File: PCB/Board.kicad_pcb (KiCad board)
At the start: 2 copper layers, 80 x 40 mm, 3 parts, among them Q2 IRF9540N, U1 ESP32-C3-SuperMini

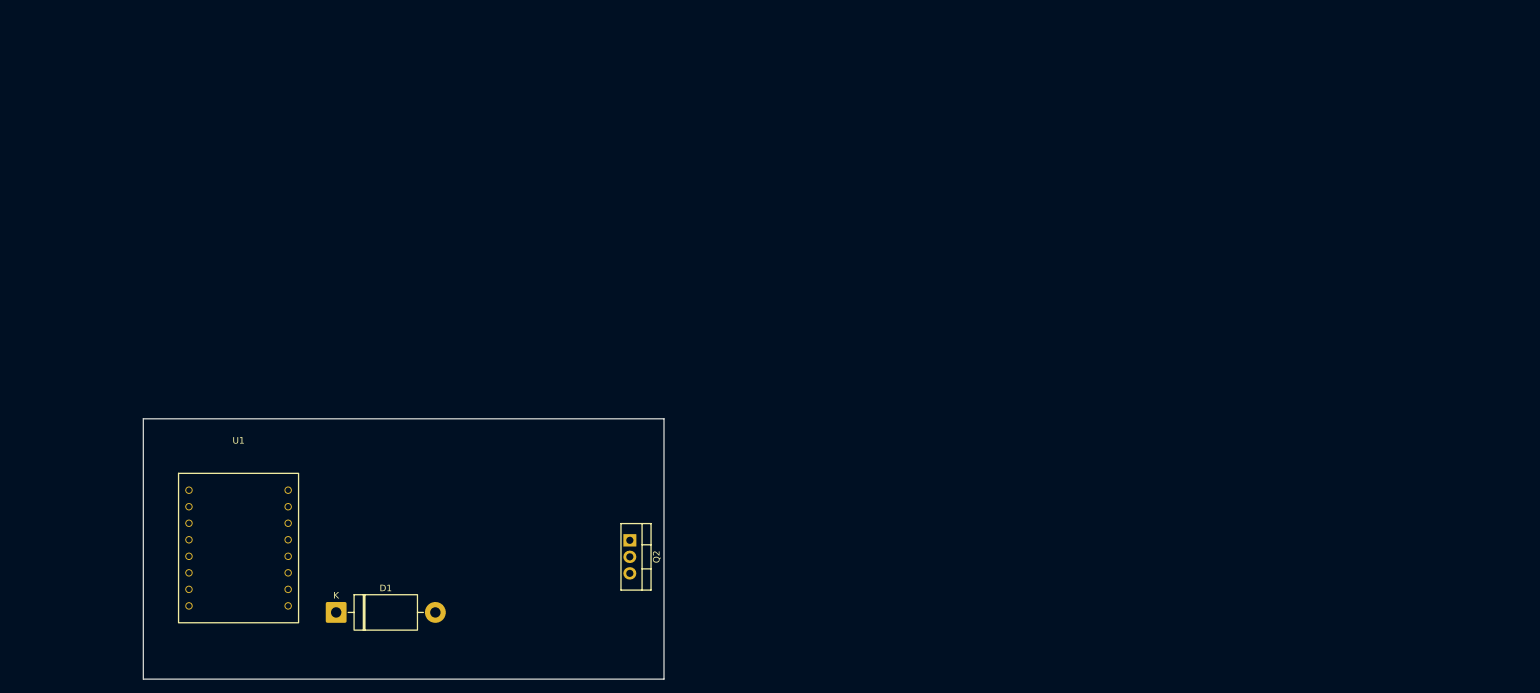
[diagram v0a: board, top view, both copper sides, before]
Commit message: PCB: fix and localize 3D models for all footprints
- Fix Q2 (SparkFun TO-220-3 footprint): model path used the
  nonexistent ${KICAD9_3RD_PARTY} env var instead of
  ${KICAD10_3RD_PARTY}, leaving it unresolved on KiCad 10.
- Fix J1 (TerminalBlock_MaiXu_MX126-5.0-02P): no 3D model exists for
  this footprint anywhere, including upstream (see kicad-packages3D
  issue #442, "Missing Terminal Blocks 3D"). Substituted the closest
  match already in KiCad's library: TerminalBlock_Phoenix
  PT-1,5-2-5.0-H (same pin count, pitch, and orientation).
- Copy every model actually used by the board (resistor, diode,
  buzzer, TO-92L, both TO-220-3 variants, IRF9Z34N, SparkFun TO-220-3,
  Phoenix terminal block, ESP32-C3-SuperMini) into PCB/3d_models/ and
  repoint all (model ...) references at ${KIPRJMOD}/3d_models/..., so
  the board no longer depends on system libraries, PCM 3rd-party
  installs, or a user's ~/Downloads folder to render correctly.
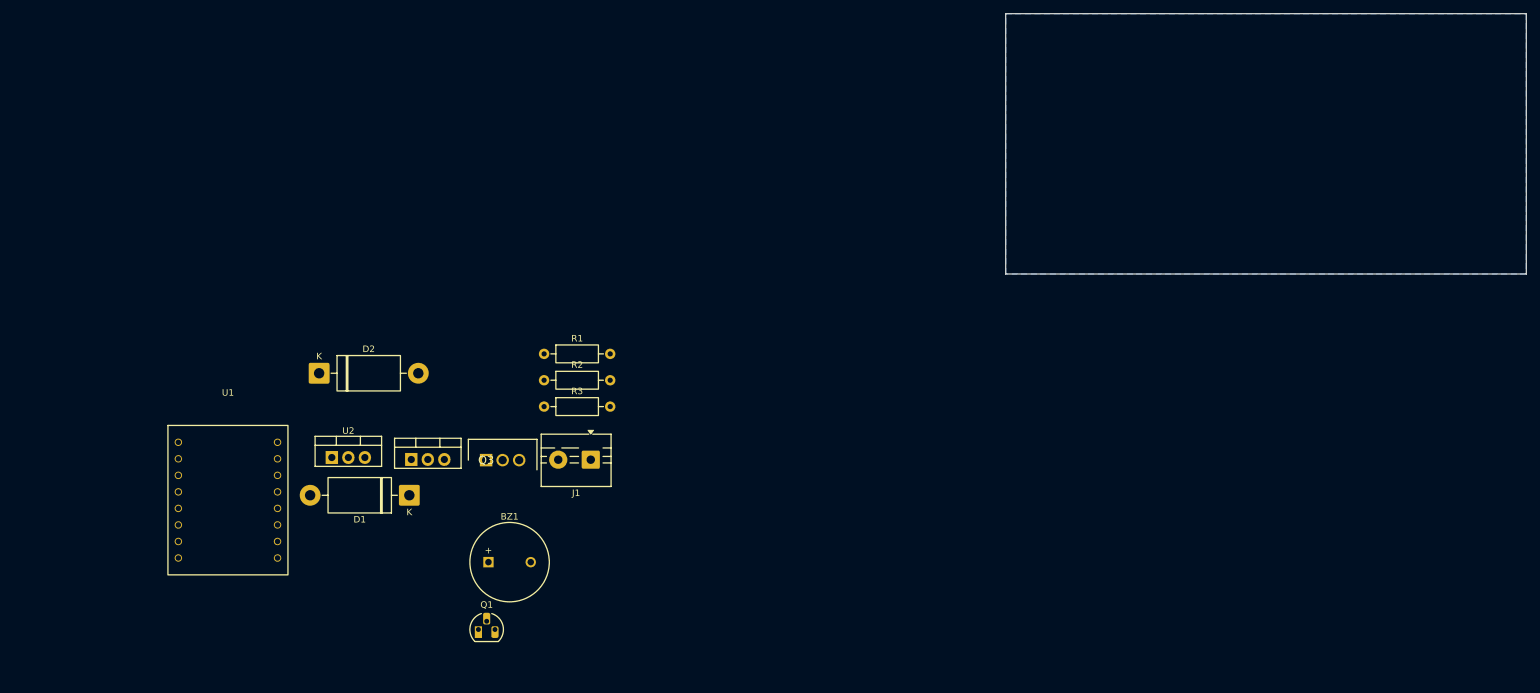
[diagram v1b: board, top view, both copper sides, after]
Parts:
- added BZ1: Buzzer_5V, Buzzer_Beeper:MagneticBuzzer_ProSignal_ABT-410-RC, F.Cu at (114.5, 108.5)
- added D2: 1N5822, Diode_THT:D_DO-201AD_P15.24mm_Horizontal, F.Cu at (88.5, 79.5)
- added J1: Screw_Terminal_01x02, TerminalBlock:TerminalBlock_MaiXu_MX126-5.0-02P_1x02_P5.00mm, F.Cu at (130.2, 92.8)
- added Q1: NPN, Package_TO_SOT_THT:TO-92L_HandSolder, F.Cu at (113.0, 118.9)
- added Q3: IRF9Z34N, PCM_IRF9Z34N:TO254P469X1042X1967-3P, F.Cu at (114.2, 92.8)
- added R1: R_US, Resistor_THT:R_Axial_DIN0207_L6.3mm_D2.5mm_P10.16mm_Horizontal, F.Cu at (123.1, 76.5)
- added R2: R_US, Resistor_THT:R_Axial_DIN0207_L6.3mm_D2.5mm_P10.16mm_Horizontal, F.Cu at (123.1, 80.6)
- added R3: R_US, Resistor_THT:R_Axial_DIN0207_L6.3mm_D2.5mm_P10.16mm_Horizontal, F.Cu at (123.1, 84.6)
- added U2: LM7805_TO220, Package_TO_SOT_THT:TO-220-3_Vertical, F.Cu at (90.5, 92.5)
- Q2: value IRF9540N -> IRLZ44N; footprint Package_TO_SOT_THT:TO-220-3_Vertical -> PCM_SparkFun-Semiconductor-Standard:TO-220-3_Vertical
- moved Q2 35.8 mm to (102.7, 92.8), turned to 0 degrees
- moved D1 21.2 mm to (102.4, 98.2), turned to 180 degrees
- moved U1 7.54 mm to (74.5, 99.0)
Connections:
- D1 pad 1: unconnected-(D1-K-Pad1) -> Net-(D1-K)
- D1 pad 2: unconnected-(D1-A-Pad2) -> GND
- Q2 pad 1: unconnected-(Q2-G-Pad1) -> DCH_PWM
- Q2 pad 2: unconnected-(Q2-D-Pad2) -> Net-(Q2-D)
- Q2 pad 3: unconnected-(Q2-S-Pad3) -> GND
- U1 pad 1: unconnected-(U1-GPIO0-Pad1) -> TEMP_ADC
- U1 pad 14: unconnected-(U1-GPIO10-Pad14) -> DCH_PWM
- U1 pad 15: unconnected-(U1-GPIO20-Pad15) -> BUZZER
- U1 pad 2: unconnected-(U1-GPIO1-Pad2) -> ENC_CLK
- U1 pad 4: unconnected-(U1-GPIO3-Pad4) -> ENC_DT
- U1 pad 5: unconnected-(U1-GPIO4-Pad5) -> ENC_SW
- U1 pad 6: unconnected-(U1-3V3-Pad6) -> +3V3
- U1 pad 8: unconnected-(U1-5V-Pad8) -> 5V
- U1 pad 9: unconnected-(U1-GPIO5-Pad9) -> CHG_PWM
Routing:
- added copper zone on B.Cu, net GND

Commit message: Added: Especificacion de los componentes del buck
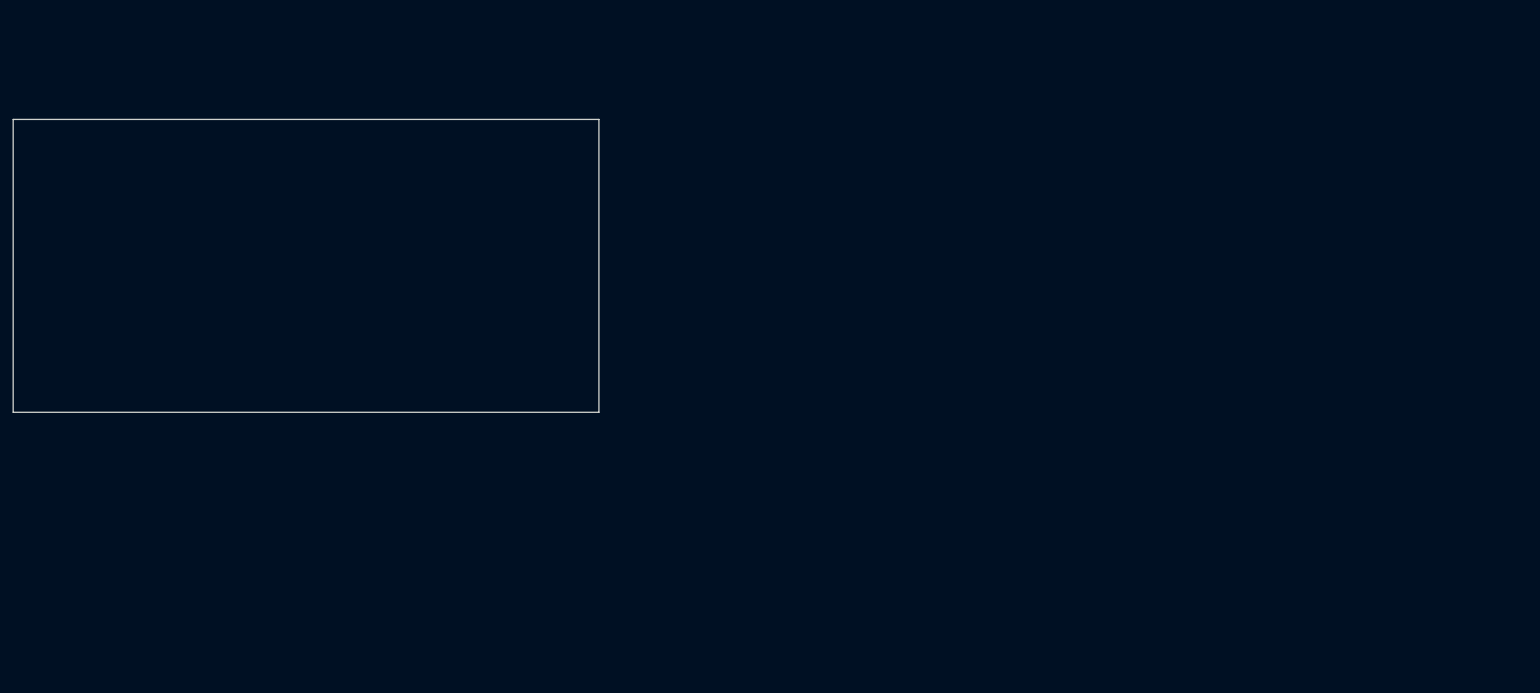
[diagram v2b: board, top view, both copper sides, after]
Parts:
- removed BZ1: Buzzer_5V, Buzzer_Beeper:MagneticBuzzer_ProSignal_ABT-410-RC
- removed D1, D2: 1N5822, Diode_THT:D_DO-201AD_P15.24mm_Horizontal
- removed J1: Screw_Terminal_01x02, TerminalBlock:TerminalBlock_MaiXu_MX126-5.0-02P_1x02_P5.00mm
- removed Q1: NPN, Package_TO_SOT_THT:TO-92L_HandSolder
- removed Q2: IRLZ44N, PCM_SparkFun-Semiconductor-Standard:TO-220-3_Vertical
- removed Q3: IRF9Z34N, PCM_IRF9Z34N:TO254P469X1042X1967-3P
- removed R1, R2, R3: R_US, Resistor_THT:R_Axial_DIN0207_L6.3mm_D2.5mm_P10.16mm_Horizontal
- removed U1: ESP32-C3-SuperMini, ESP32C3SM:ESP32-C3-SuperMini
- removed U2: LM7805_TO220, Package_TO_SOT_THT:TO-220-3_Vertical
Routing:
- removed copper zone on B.Cu, net GND
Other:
- board size 80 x 40 mm -> 90 x 45 mm
